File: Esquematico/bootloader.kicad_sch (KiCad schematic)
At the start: 18 parts

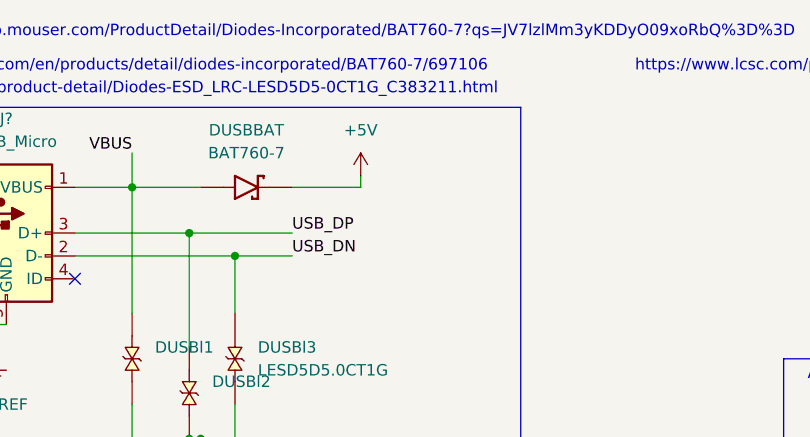
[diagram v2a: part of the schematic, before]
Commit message: Agregado circuito de potencia a través de Jack y selector de posición para alimentar de USB, Jack o apagar
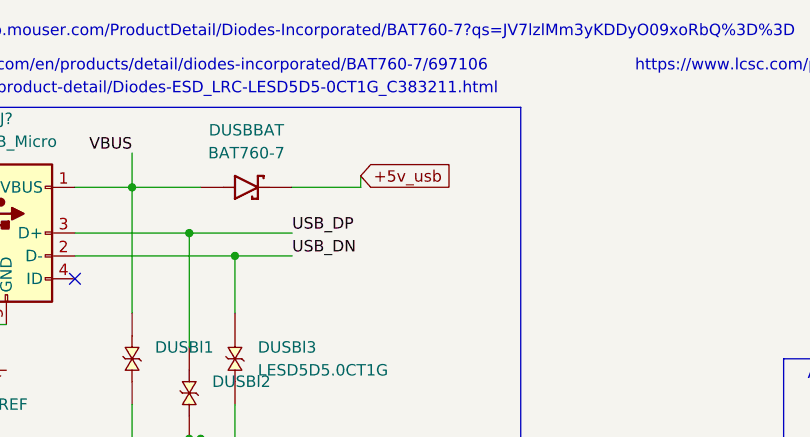
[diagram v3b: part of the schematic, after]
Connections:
- net +5V renamed +5v_usb
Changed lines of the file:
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@@
     (effects (font (size 1.27 1.27)) (justify right bottom))
+  )
+  (global_label "+5v_usb" (shape input) (at 73.66 33.02 0) (fields_autoplaced)
+    (effects (font (size 1.27 1.27)) (justify left))
+    (property "Intersheet References" "${INTERSHEET_REFS}" (id 0) (at 84.1164 32.9406 0)
+      (effects (font (size 1.27 1.27)) (justify left) hide)
+    )
   )
   (global_label "EN" (shape passive) (at 77.47 140.97 0) (fields_autoplaced)
@@
       (effects (font (size 1.27 1.27)) hide)
     )
-    (pin "1")
-  )
-  (symbol (lib_id "power:+5V") (at 73.66 33.02 0) (unit 1)
-    (in_bom yes) (on_board yes) (fields_autoplaced)
-    (property "Reference" "#PWR?" (id 0) (at 73.66 36.83 0)
-      (effects (font (size 1.27 1.27)) hide)
-    )
-    (property "Value" "+5V" (id 1) (at 73.66 27.94 0))
-    (property "Footprint" "" (id 2) (at 73.66 33.02 0)
-      (effects (font (size 1.27 1.27)) hide)
-    )
-    (property "Datasheet" "" (id 3) (at 73.66 33.02 0)
-      (effects (font (size 1.27 1.27)) hide)
-    )

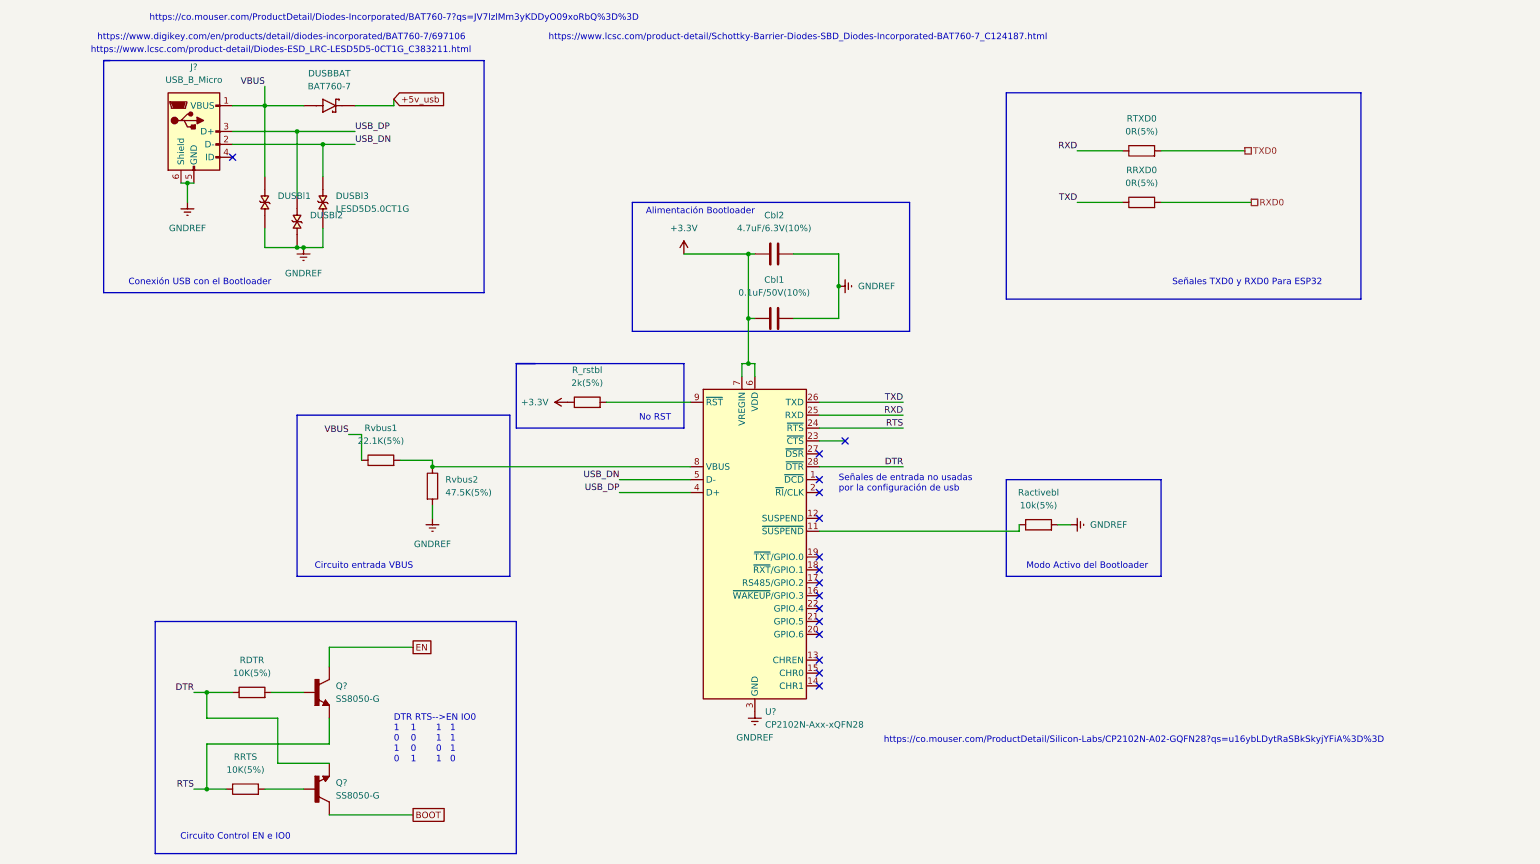
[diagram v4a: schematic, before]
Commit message: actualizacion huellas resitencias y capacitorees
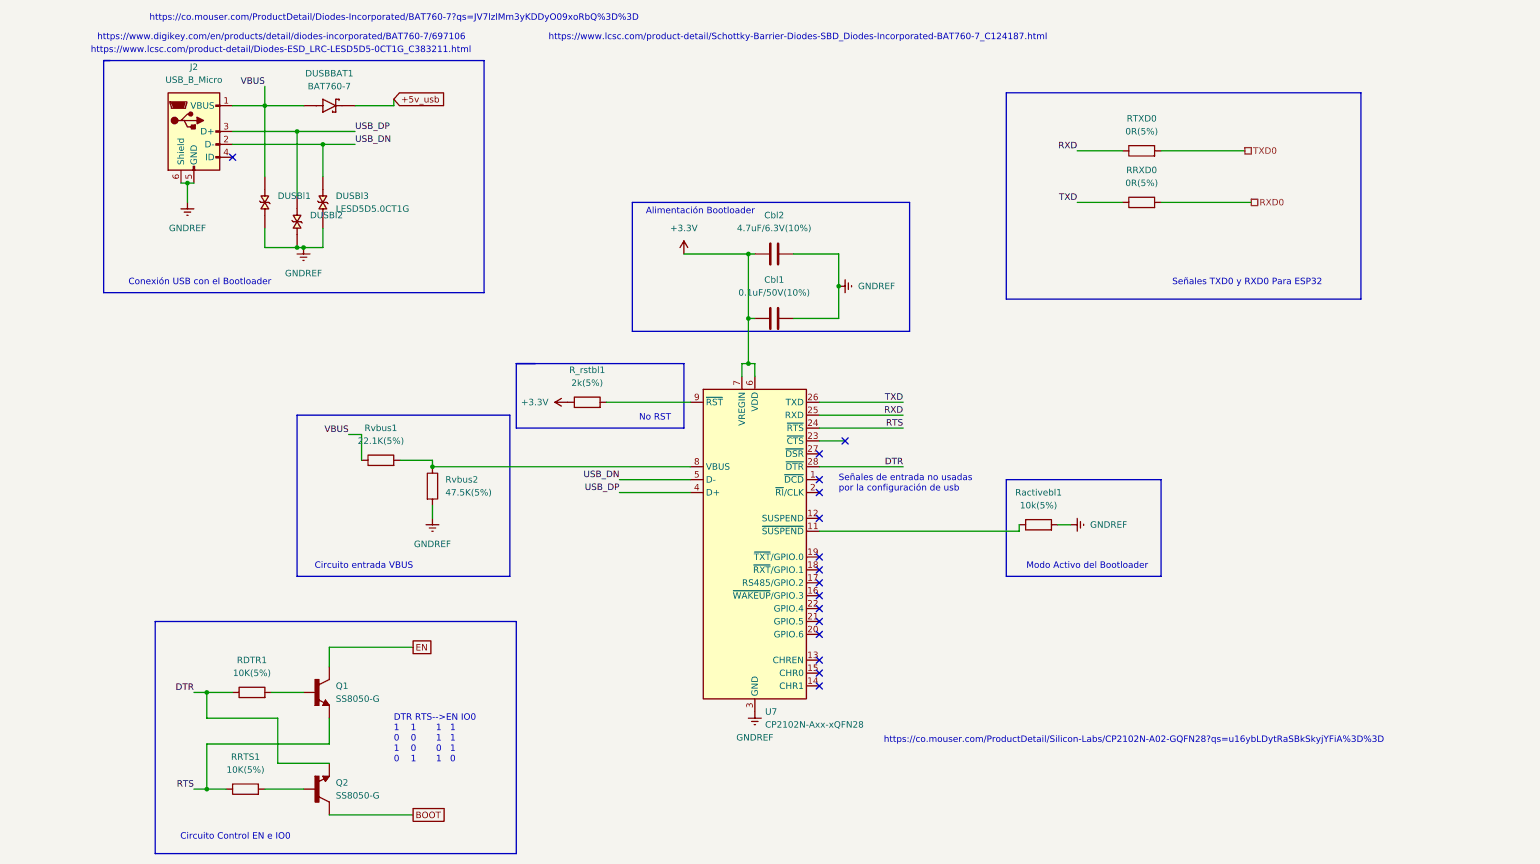
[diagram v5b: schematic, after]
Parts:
- Cbl1, Cbl2: footprint (none) -> Capacitor_SMD:C_0805_2012Metric_Pad1.18x1.45mm_HandSolder
- DUSBl1, DUSBl2, DUSBl3: footprint TVS_LESD5D5.0CT1G -> LESD5D5:TVS_LESD5D5.0CT1G
- J2: renamed from J?; footprint (none) -> Connector_USB:USB_Micro-B_Wuerth_629105150521
- Q1, Q2: renamed from Q?; footprint TRANS_SS8050-G -> SS8050-G:TRANS_SS8050-G
- RDTR1: renamed from RDTR; footprint (none) -> Resistor_SMD:R_0805_2012Metric_Pad1.20x1.40mm_HandSolder
- RRTS1: renamed from RRTS; footprint (none) -> Resistor_SMD:R_0805_2012Metric_Pad1.20x1.40mm_HandSolder
- RRXD0, RTXD0, Rvbus1, Rvbus2: footprint (none) -> Resistor_SMD:R_0805_2012Metric_Pad1.20x1.40mm_HandSolder
- R_rstbl1: renamed from R_rstbl; footprint (none) -> Resistor_SMD:R_0805_2012Metric_Pad1.20x1.40mm_HandSolder
- Ractivebl1: renamed from Ractivebl; footprint (none) -> Resistor_SMD:R_0805_2012Metric_Pad1.20x1.40mm_HandSolder
- gave numbers to parts that had none: 1
- renumbered DUSBBAT to DUSBBAT1
